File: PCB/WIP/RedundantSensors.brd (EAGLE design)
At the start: 111.7 x 100 mm, 176 parts, among them J1 10118192-0001LF, J3 503182-1852, J4 JST-SH-4_SMT_V, U1 TPD4F003DQDR, U10 LIS3MDLTR, U2 BMI088, U3 BMI088, U4 BMI088, U5 STM32H743ZIT6, U6 LIS3MDLTR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

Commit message: PCB update
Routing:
- net N$27: track 16.2 -> 17.2 mm
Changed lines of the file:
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@@
 <wire x1="68.58" y1="74.2782875" x2="68.58" y2="78.74" width="0.1524" layer="1"/>
 <via x="68.58" y="78.74" extent="1-16" drill="0.35"/>
-<wire x1="68.58" y1="78.74" x2="73.66" y2="78.74" width="0.1524" layer="16"/>
+<wire x1="72.39" y1="77.47" x2="69.85" y2="77.47" width="0.1524" layer="16"/>
+<wire x1="68.58" y1="78.74" x2="69.85" y2="77.47" width="0.1524" layer="16"/>
+<wire x1="72.39" y1="77.47" x2="73.66" y2="78.74" width="0.1524" layer="16"/>
 <via x="73.66" y="78.74" extent="1-16" drill="0.35"/>
 <wire x1="73.66" y1="78.74" x2="72.62" y2="79.78" width="0.1524" layer="1"/>

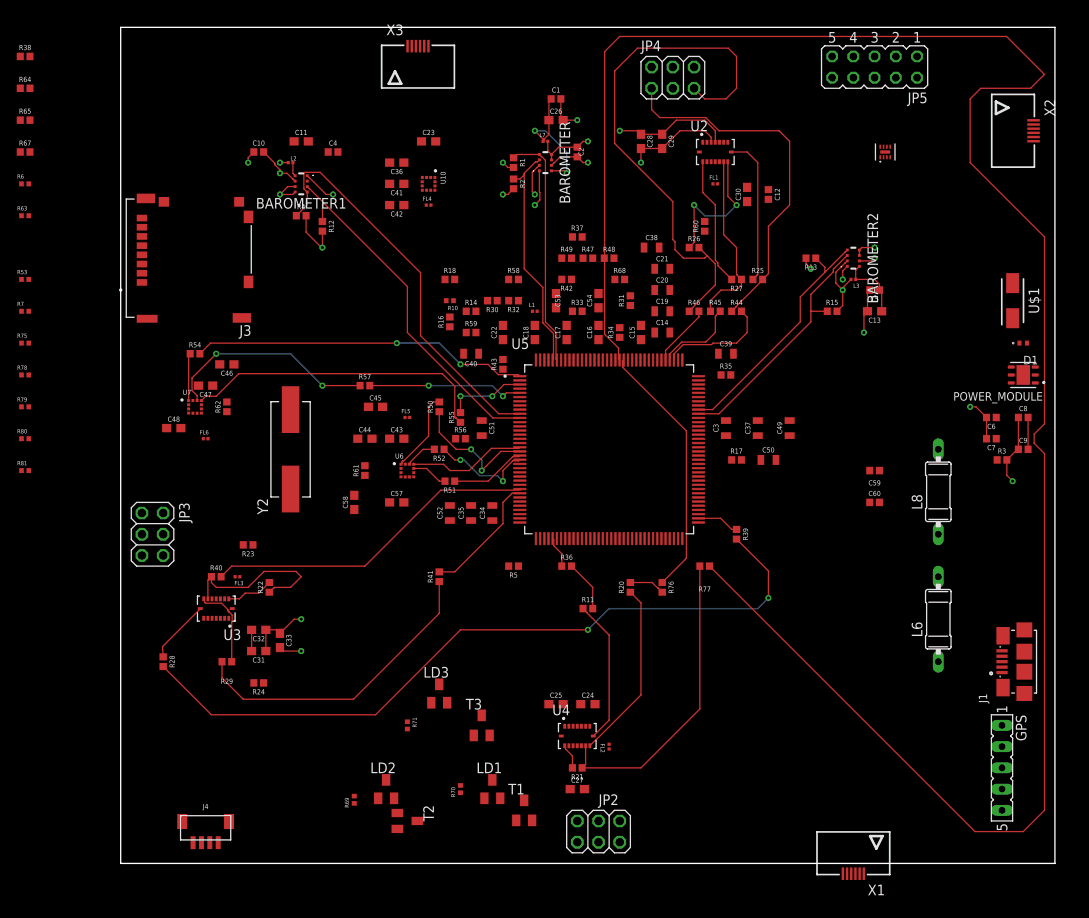
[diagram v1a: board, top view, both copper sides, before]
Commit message: PCB with I2C + SPI connected
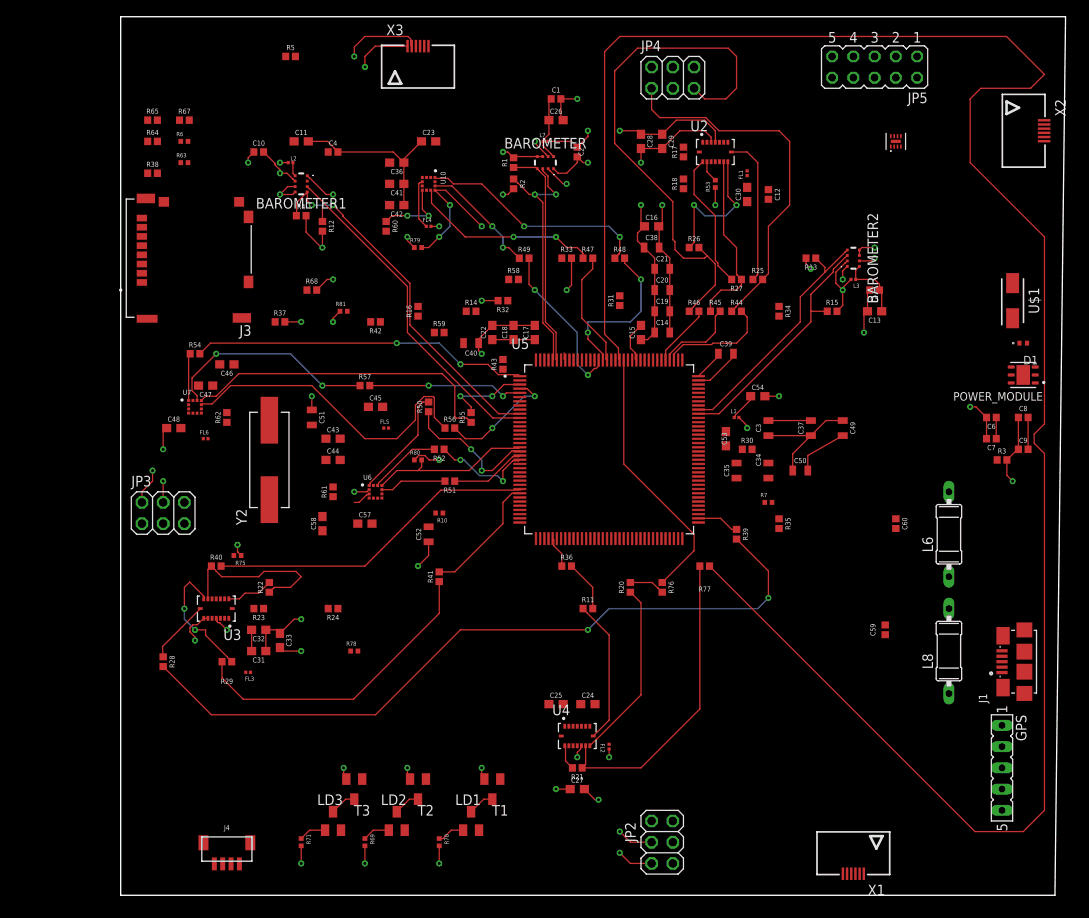
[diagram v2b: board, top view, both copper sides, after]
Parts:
- moved R7 91.8 mm to (77.5, 43.2)
- moved R53 83.3 mm to (71.1, 81.3), turned to 90 degrees
- moved R5 66.5 mm to (20.3, 96.5), turned to 0 degrees
- moved R78 51.4 mm to (27.9, 25.4)
- moved R79 50.7 mm to (35.6, 73.7)
- moved R80 47.1 mm to (35.6, 48.3)
- moved R81 42.6 mm to (26.7, 66.0)
- moved R60 38.1 mm to (31.8, 76.2), turned to 270 degrees
- moved R17 37.4 mm to (67.3, 85.1), turned to 90 degrees
- moved R37 37.0 mm to (19.1, 64.8)
- moved R68 36.9 mm to (22.9, 68.6)
- moved R75 35.9 mm to (14.0, 36.8), turned to 180 degrees
- moved R30 35.3 mm to (74.9, 49.5), turned to 0 degrees
- moved C34 33.4 mm to (77.5, 47.0)
- moved C35 32.2 mm to (73.7, 47.0)
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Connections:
- net LED03: now also U5.48; no longer U5.96
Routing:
- net GND: track 63.1 -> 167.4 mm, vias 11 -> 28
- net 3V3: track 52.0 -> 125.1 mm, vias 13 -> 33
- net SPI4_MISO: track 0.00 -> 38.8 mm
- net SPI6_SCK: track 0.00 -> 27.8 mm, vias 0 -> 2
- net SPI6_MISO: track 0.00 -> 22.8 mm, vias 0 -> 2
- net N$46: track 0.00 -> 19.3 mm, vias 0 -> 2
- net N$45: track 0.00 -> 19.3 mm, vias 0 -> 2
- net SPI6_CS: track 0.00 -> 16.9 mm, vias 0 -> 3
- net AGND: track 0.00 -> 14.6 mm
- net SPI6_MOSI: track 0.00 -> 14.4 mm, vias 0 -> 2
- net N$14: track 0.00 -> 14.4 mm, vias 0 -> 2
- net N$44: track 0.00 -> 14.0 mm
- net VREFP: track 0.00 -> 9.97 mm
- net N$56: track 0.00 -> 8.72 mm, vias 0 -> 2
- net N$6: track 16.5 -> 7.82 mm, vias 2 -> 0
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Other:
- board size 111.7 x 100 mm -> 113 x 105.1 mm

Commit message: edison autoroute
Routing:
- net 5V: track 2.54 -> 251.3 mm
- net GND: track 167.4 -> 385.0 mm, vias 28 -> 46
- net 3V3: track 125.1 -> 287.1 mm, vias 33 -> 47
- net USART2_RX: track 0.00 -> 125.9 mm, vias 0 -> 2
- net DRDY2_GYRO3: track 0.00 -> 125.5 mm, vias 0 -> 2
- net 5V_IN: track 0.00 -> 108.2 mm, vias 0 -> 2
- net UART8_RX: track 0.00 -> 107.9 mm, vias 0 -> 2
- net CSB_ACCEL4: track 0.00 -> 107.8 mm, vias 0 -> 3
- net SDMCC_D1: track 0.00 -> 104.2 mm, vias 0 -> 4
- net UART5_TX: track 0.00 -> 103.6 mm, vias 0 -> 4
- net SDMCC_D0: track 0.00 -> 100.9 mm, vias 0 -> 3
- net NRST: track 0.00 -> 100.3 mm, vias 0 -> 6
- net CSB_GYRO1: track 0.00 -> 99.8 mm, vias 0 -> 4
- net N$20: track 0.00 -> 98.0 mm, vias 0 -> 2
- net SDMCC_CMD: track 0.00 -> 93.5 mm, vias 0 -> 4
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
